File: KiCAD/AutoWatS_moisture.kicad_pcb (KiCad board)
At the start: 2 copper layers, 16.5 x 138 mm, 20 parts, among them J1 Conn_02x03_Odd_Even, J2 Conn_01x04, U1 ATtiny441-SSU, Y1 YSX321SL

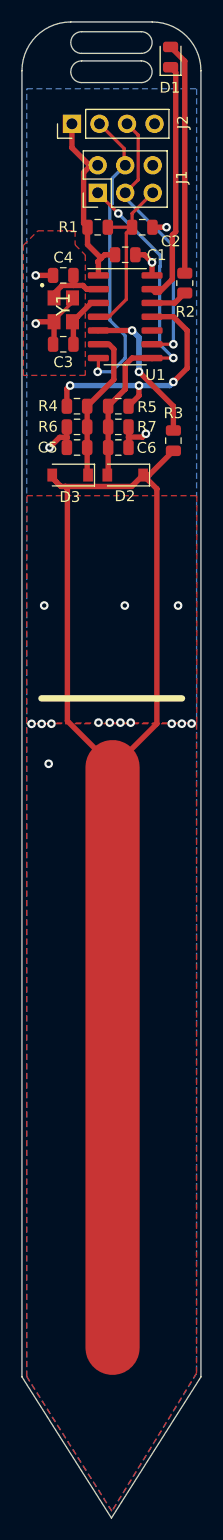
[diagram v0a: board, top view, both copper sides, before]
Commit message: Added debug port, silk info and changed the layout a bit
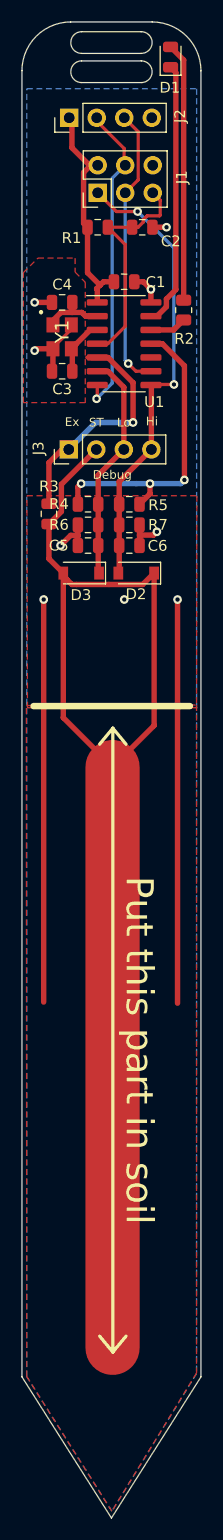
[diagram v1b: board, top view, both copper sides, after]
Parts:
- added J3: Conn_01x04, Connector_PinHeader_2.54mm:PinHeader_1x04_P2.54mm_Vertical, F.Cu at (113.5, 71.9)
- moved R3 13.3 mm to (111.7, 77.9)
- moved C5 9.10 mm to (115.3, 80.8)
- moved C6 9.10 mm to (119.1, 80.8)
- moved R4 9.10 mm to (115.3, 77.0)
- moved R5 9.10 mm to (119.1, 77.0)
- moved R6 9.10 mm to (115.3, 78.9)
- moved R7 9.10 mm to (119.1, 78.9)
- moved D2 9.10 mm to (119.8, 83.3)
- moved D3 9.10 mm to (114.7, 83.3)
- moved C3 2.49 mm to (112.9, 64.7)
- moved U1 2.49 mm to (118.6, 62.2)
- moved R2 2.49 mm to (124.1, 59.1)
- moved C1 2.49 mm to (118.6, 56.5)
- moved C4 2.49 mm to (112.9, 58.4)
- moved Y1 2.49 mm to (112.9, 61.5)
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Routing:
- net GND: track 20.8 -> 95.2 mm, vias 20 -> 9
- net /MISO_SENSE_HIGH: track 33.7 -> 44.2 mm
- net /Excitation: track 14.5 -> 23.3 mm, vias 2 -> 1
- net /SENSE_LOW: track 14.8 -> 22.6 mm
- net /SENSOR_TRACK: track 123.6 -> 116.1 mm
- net /POWER: track 23.0 -> 28.5 mm
- net /RESET: track 16.3 -> 20.8 mm
- net VCC: track 18.6 -> 21.0 mm
- net Net-(D1-Pad2): track 21.5 -> 23.9 mm
- net Net-(D1-Pad1): track 22.4 -> 24.4 mm
- net /SCK_SCL: track 25.1 -> 26.7 mm
- net /MOSI_SDA: track 28.1 -> 28.7 mm
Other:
- board text added: "Debug"
- board text added: "Ex"
- board text added: "Hi"
- board text added: "Lo"
- board text added: "Put this part in soil"
- board text added: "ST"
